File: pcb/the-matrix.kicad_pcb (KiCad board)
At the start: 4 copper layers, 102 x 102 mm, 81 parts, among them J1 DNP, J2 DNP, J3 Conn_02x20_Odd_Even, J4 Conn_02x20_Odd_Even, J5 Conn_02x20_Odd_Even, J6 Conn_02x20_Odd_Even, Q1 Q_PMOS_GDS, Q10 Q_PMOS_GDS, Q11 Q_PMOS_GDS, Q12 Q_PMOS_GDS, Q13 Q_PMOS_GDS, Q14 Q_PMOS_GDS, Q15 Q_PMOS_GDS, Q16 Q_PMOS_GDS, Q17 Q_PMOS_GDS, Q18 Q_PMOS_GDS, Q19 Q_PMOS_GDS, Q2 Q_PMOS_GDS, Q20 Q_PMOS_GDS, Q21 Q_PMOS_GDS, Q22 Q_PMOS_GDS, Q23 Q_PMOS_GDS, Q24 Q_PMOS_GDS, Q25 Q_PMOS_GDS, Q26 Q_PMOS_GDS, Q27 Q_PMOS_GDS, Q28 Q_PMOS_GDS, Q29 Q_PMOS_GDS, Q3 Q_PMOS_GDS, Q30 Q_PMOS_GDS, Q31 Q_PMOS_GDS, Q32 Q_PMOS_GDS, Q33 Q_PMOS_GDS, Q34 Q_PMOS_GDS, Q35 Q_PMOS_GDS, Q36 Q_PMOS_GDS, Q37 Q_PMOS_GDS, Q38 Q_PMOS_GDS, Q39 Q_PMOS_GDS, Q4 Q_PMOS_GDS, Q40 Q_PMOS_GDS, Q5 Q_PMOS_GDS, Q6 Q_PMOS_GDS, Q7 Q_PMOS_GDS, Q8 Q_PMOS_GDS, Q9 Q_PMOS_GDS, U1 74HC595, U10 TPIC6B595N, U2 74HC595, U3 74HC595, U4 74HC595, U5 74HC595, U6 TPIC6B595N, U7 TPIC6B595N, U8 TPIC6B595N, U9 TPIC6B595N

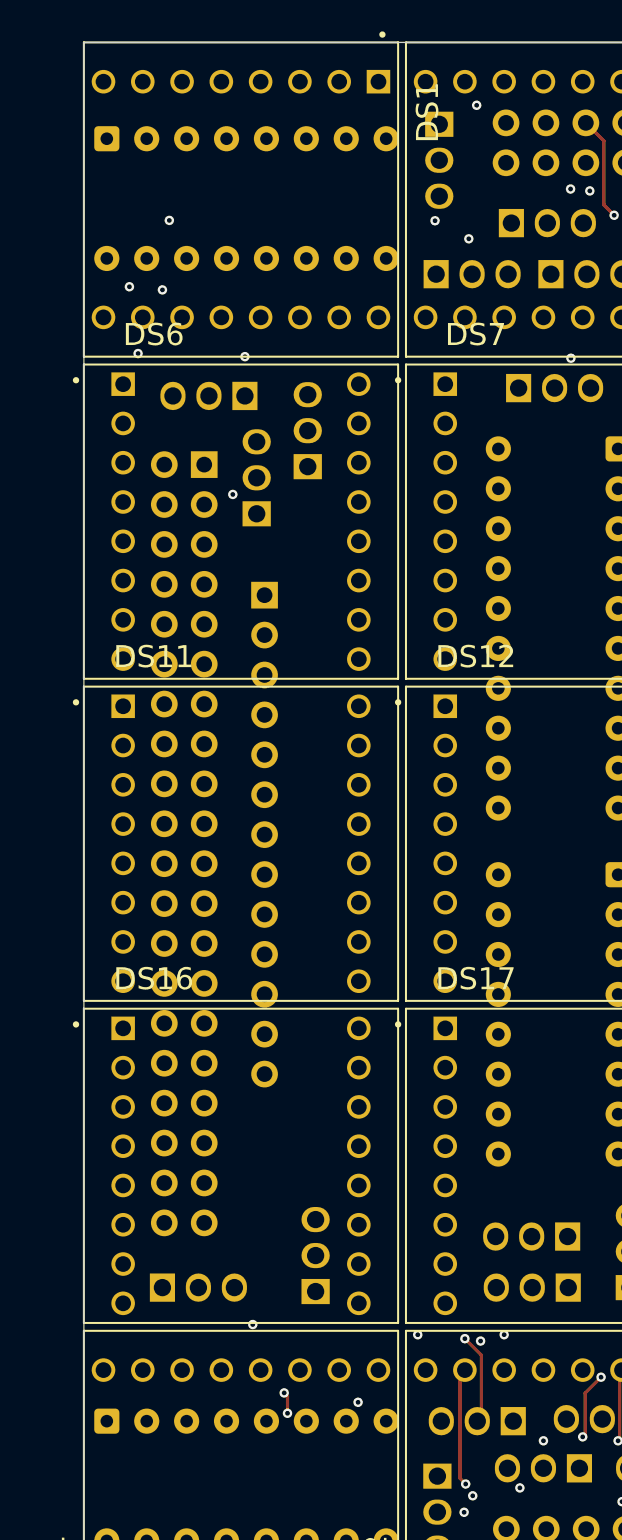
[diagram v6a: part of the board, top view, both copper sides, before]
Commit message: route the left connector
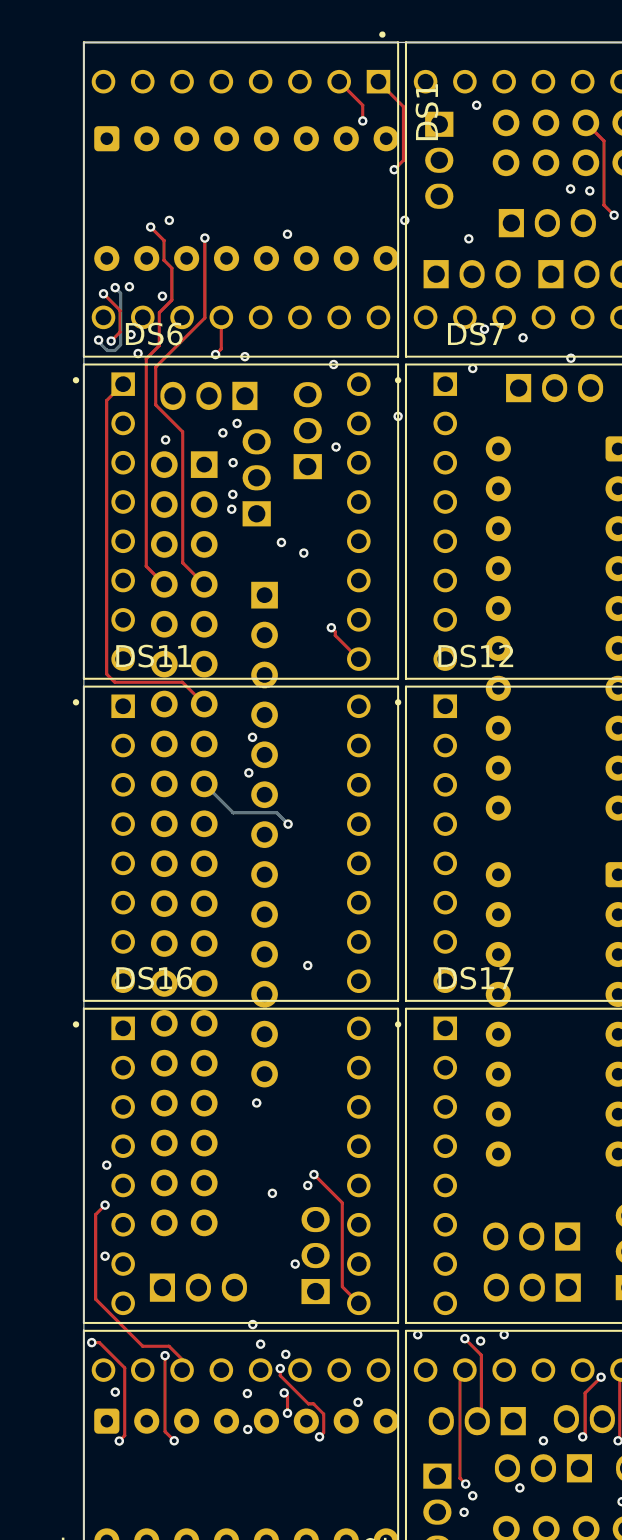
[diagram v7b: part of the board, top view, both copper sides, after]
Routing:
- net /ROWA1: track 66.4 -> 110.2 mm, vias 0 -> 4
- net /ROWA6: track 95.0 -> 137.4 mm, vias 0 -> 3
- net /ROWA3: track 69.0 -> 108.9 mm, vias 0 -> 4
- net /ROWA4: track 89.8 -> 129.4 mm, vias 0 -> 2
- net /ROWA0: track 65.6 -> 101.6 mm, vias 0 -> 1
- net /ROWA7: track 88.7 -> 124.3 mm, vias 0 -> 1
- net /ROWA5: track 101.2 -> 136.7 mm, vias 0 -> 2
- net /ROWA36: track 87.1 -> 121.4 mm, vias 0 -> 2
- net /ROWA38: track 89.6 -> 123.5 mm, vias 0 -> 1
- net /ROWA2: track 95.6 -> 129.5 mm, vias 0 -> 2
- net /ROWA37: track 101.8 -> 135.3 mm, vias 0 -> 3
- net /ROWA39: track 96.7 -> 128.7 mm, vias 0 -> 3
- net /ROWA34: track 109.1 -> 140.6 mm, vias 0 -> 2
- net /ROWA12: track 87.6 -> 118.7 mm
- net /ROWA14: track 86.2 -> 115.9 mm, vias 0 -> 3
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
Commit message: connectors complete!
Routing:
- net /ROWA7: track 124.3 -> 176.8 mm, vias 1 -> 4
- net /ROWA26: track 112.2 -> 161.7 mm, vias 1 -> 8
- net /ROWA36: track 121.4 -> 166.3 mm, vias 2 -> 5
- net /ROWA6: track 137.4 -> 180.0 mm, vias 3 -> 4
- net /ROWA38: track 123.5 -> 164.3 mm, vias 1 -> 4
- net /ROWA2: track 129.5 -> 169.3 mm, vias 2 -> 5
- net /ROWA4: track 129.4 -> 167.9 mm, vias 2 -> 4
- net /ROWA37: track 135.3 -> 173.8 mm, vias 3 -> 6
- net /ROWA12: track 118.7 -> 157.0 mm, vias 0 -> 2
- net /ROWA27: track 109.7 -> 146.1 mm, vias 1 -> 4
- net /ROWA34: track 140.6 -> 176.8 mm, vias 2 -> 4
- net /ROWA14: track 115.9 -> 151.6 mm, vias 3 -> 6
- net /ROWA5: track 136.7 -> 170.1 mm, vias 2 -> 4
- net /ROWA39: track 128.7 -> 160.6 mm, vias 3 -> 5
- net /ROWA24: track 115.3 -> 142.1 mm, vias 1 -> 2
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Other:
- board text added: "the matrix v1 rivques 2025 https:/github.com/ rivques/the-matrix"
- board text removed: "the matrix v1 rivques 2025"
